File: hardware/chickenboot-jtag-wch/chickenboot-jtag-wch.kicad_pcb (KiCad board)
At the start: 2 copper layers, 29 x 18 mm, 27 parts, among them J1 USB_C_Receptacle_USB2.0, J2 Conn_01x03, J3 JTAG, J4 Conn_01x03, Q1 LP0404N3T5G, SW2 SW_Push, U1 CH32X035F8U6, U2 HT7533-1, U3 USBLC6-2P6, U4 IS25WP016D-JULE-TR, U5 IS25WP016D-JULE-TR

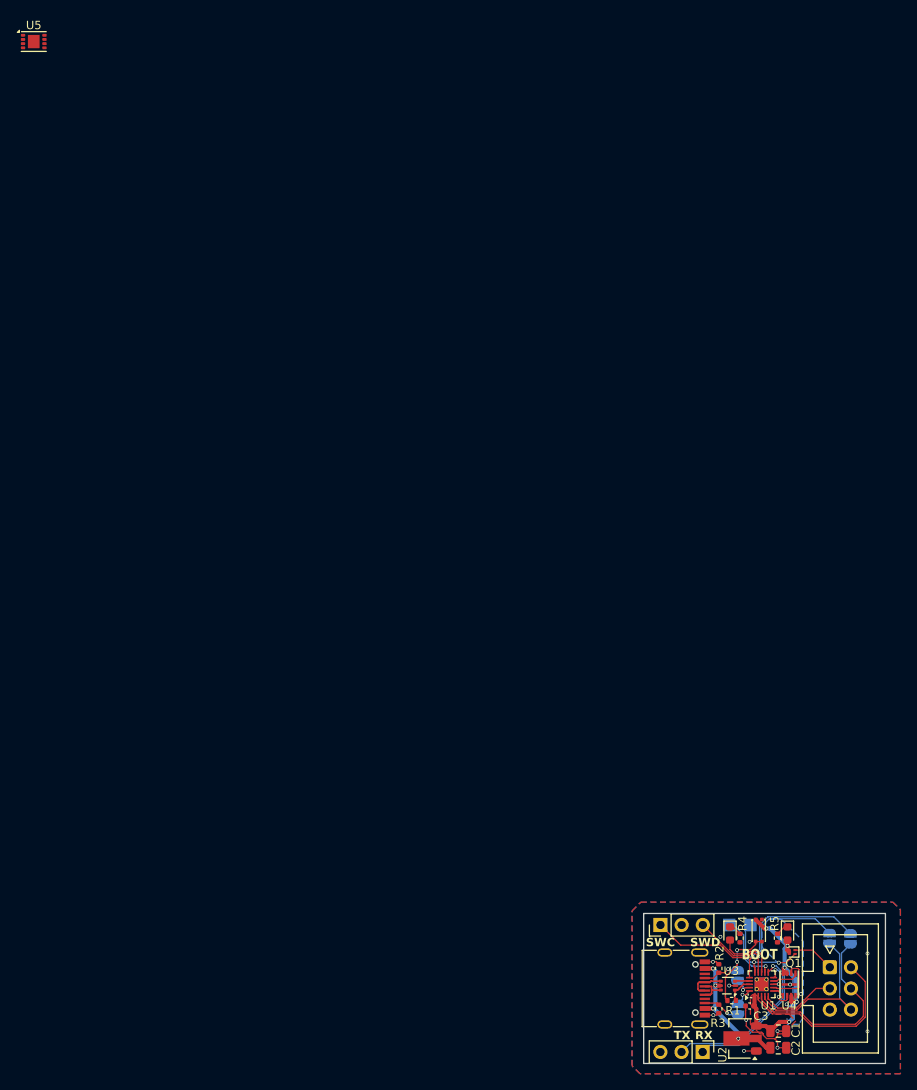
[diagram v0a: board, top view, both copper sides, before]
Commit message: add a decouliping capacitor to flash, a pullup to PMOS power control, and clean schematics
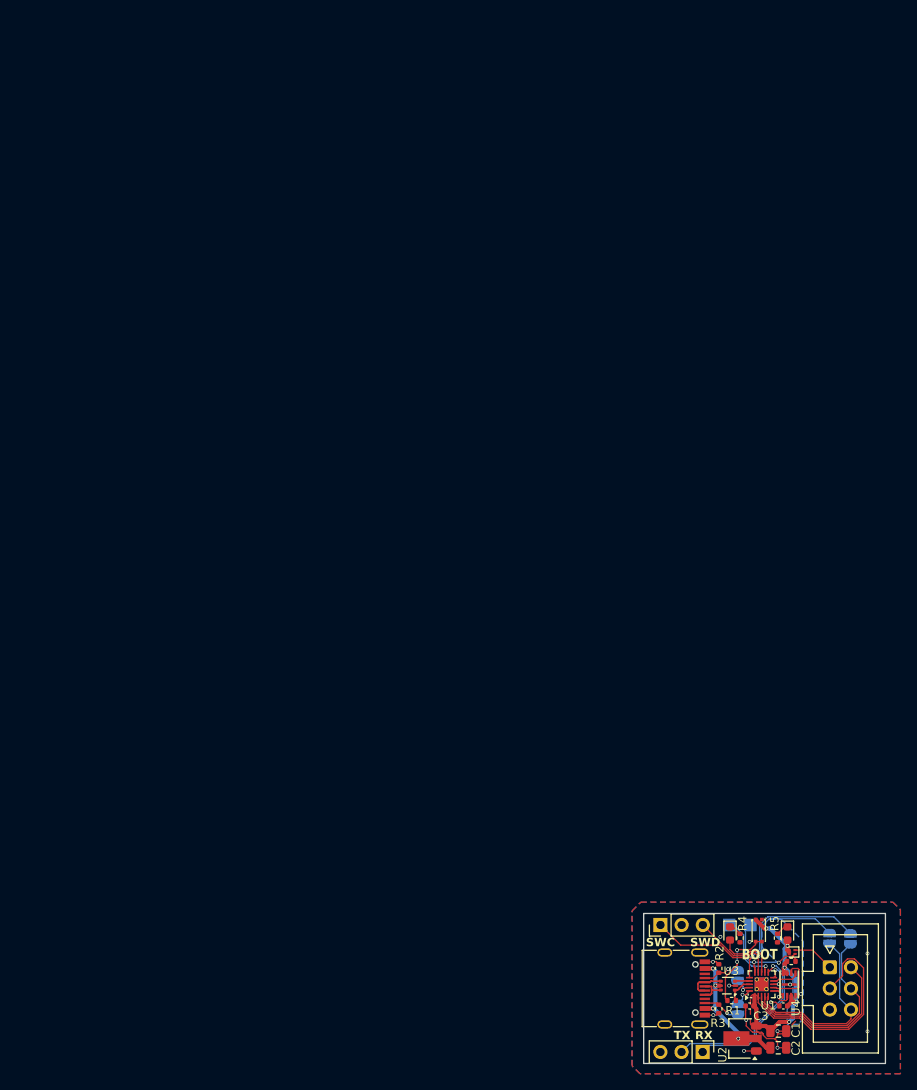
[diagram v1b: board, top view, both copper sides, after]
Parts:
- removed U5: IS25WP016D-JULE-TR, Package_SON:SON-8-1EP_3x2mm_P0.5mm_EP1.4x1.6mm
- added C4: .1uF, Capacitor_SMD:C_0402_1005Metric, F.Cu at (92.0, 117.2)
- added R6: 5.1K 1%, Resistor_SMD:R_0402_1005Metric, F.Cu at (93.0, 111.8)
- SW2: value SW_Push -> BOOT
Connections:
- net CC1 renamed /CC1
- net CC2 renamed /CC2
- net Net-(JP1-B) renamed /CC1_MCU
- net Net-(JP2-B) renamed /CC2_MCU
- net Net-(LED1-A) renamed /LED_STATUS
- U1 pad 2: JTAG_TMS -> JTAG_TDI
- U1 pad 3: JTAG_TCK -> JTAG_TMS
- U1 pad 4: JTAG_TDO -> JTAG_TCK
- U1 pad 5: JTAG_TDI -> JTAG_TDO
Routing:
- net JTAG_TDI: track 9.09 -> 27.9 mm
- net JTAG_TMS: track 23.0 -> 20.8 mm
- net +3V3: track 27.7 -> 29.3 mm
- net GND: track 17.7 -> 18.9 mm
- net JTAG_TDO: track 21.2 -> 22.3 mm
- net JTAG_TCK: track 24.4 -> 23.5 mm
- net /VTARGET_OFF: track 12.1 -> 12.8 mm
- net /RX: track 18.3 -> 18.9 mm
- net /TX: track 19.7 -> 20.4 mm
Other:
- board text added: "JTAG v0.1"
- board text removed: "JTAG v0.09"

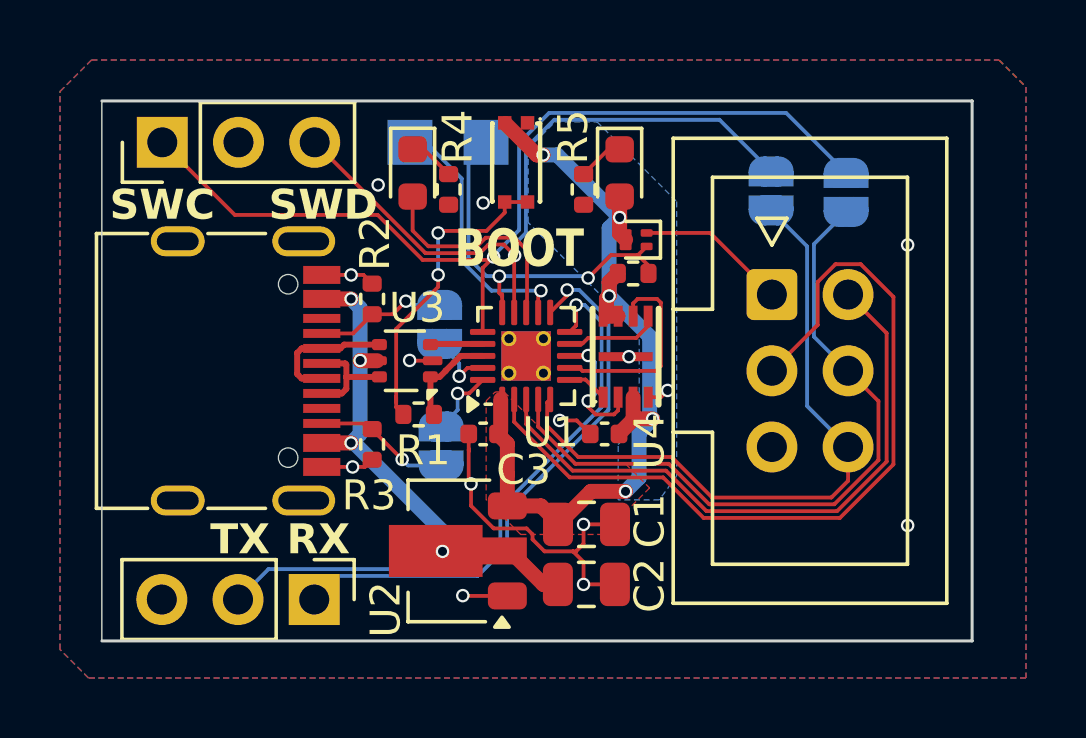
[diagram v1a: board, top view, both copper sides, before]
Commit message: change boards shape and fixes for manufacturability
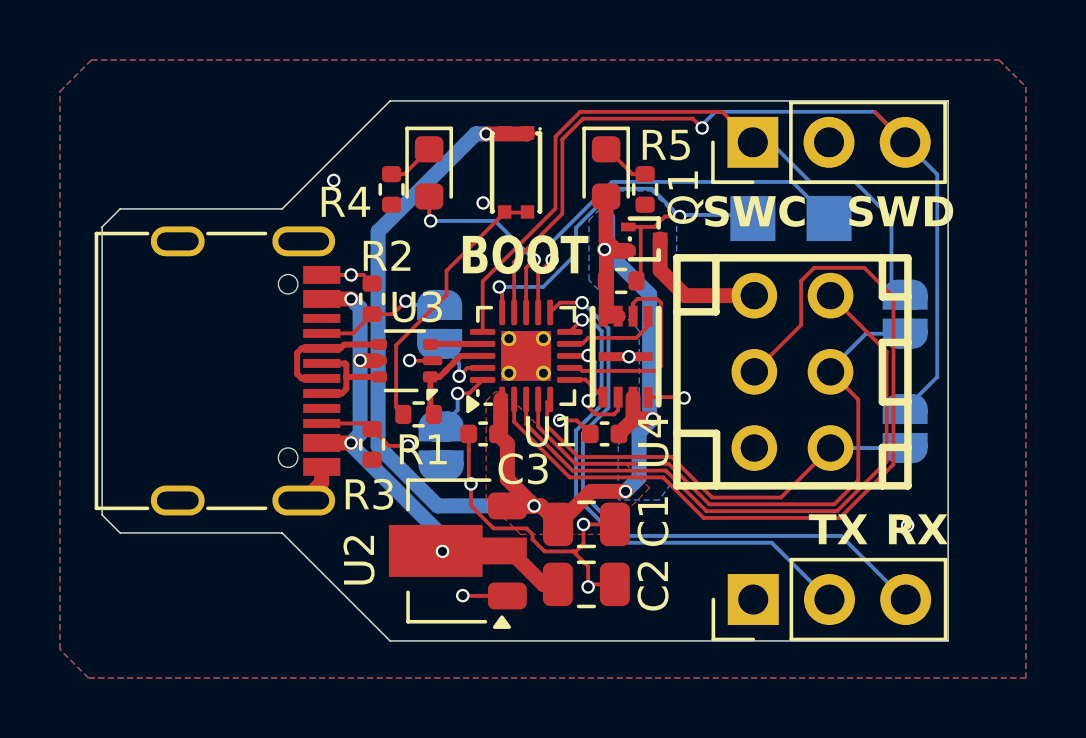
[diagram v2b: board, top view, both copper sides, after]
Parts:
- removed J3: JTAG, Connector_IDC:IDC-Header_2x03_P2.54mm_Vertical
- removed SW2: BOOT, easyeda2kicad:SW-SMD_4P-L2.5-W1.6-LS2.9_STI-055A12AX
- added CN1: 69168-106HLF, easyeda2kicad:CONN-TH_6P-P2.54_69168-X06, F.Cu at (98.3, 115.1)
- added SW1: SW_Push, easyeda2kicad:SW-SMD_4P-L2.5-W1.6-LS2.9_STI-055A12AX, F.Cu at (89.1, 108.4)
- Q1: value LP0404N3T5G -> WPM2093-3/TR; footprint Package_TO_SOT_SMD:SOT-883 -> easyeda2kicad:SOT-723_L1.2-W0.8-P0.80-LS1.2-BR
- moved J2 19.7 mm to (96.9, 107.4)
- moved J4 14.6 mm to (97.0, 122.7), turned to 90 degrees
- moved TP1 14.2 mm to (99.5, 110.0)
- moved TP2 9.25 mm to (96.9, 110.0)
- moved JP3 9.09 mm to (102.0, 117.0)
- moved JP4 4.51 mm to (102.0, 113.2)
- moved R5 2.05 mm to (93.4, 109.0)
- moved R4 1.90 mm to (84.9, 109.0)
- moved LED1 0.55 mm to (86.2, 108.5)
- moved R6 0.47 mm to (92.6, 112.1)
- moved LED2 0.45 mm to (92.1, 108.5)
- moved Q1 0.27 mm to (93.3, 110.7)
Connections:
- J4 pad 1: /RX -> GND
- J4 pad 3: GND -> /RX
- Q1 pad 2: TARGET_VCC -> +3V3
- Q1 pad 3: +3V3 -> TARGET_VCC
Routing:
- net +3V3: track 29.3 -> 47.2 mm
- net /SWCLK: track 31.7 -> 23.3 mm, vias 1 -> 0
- net JTAG_TDO: track 22.3 -> 14.6 mm
- net /SWDIO: track 23.4 -> 30.2 mm
- net /QSPI_CLOCK: track 8.84 -> 13.1 mm
- net JTAG_TCK: track 23.5 -> 20.0 mm
- net /TX: track 20.4 -> 17.1 mm
- net /VTARGET_OFF: track 12.8 -> 15.3 mm
- net /RX: track 18.9 -> 20.5 mm
- net Net-(R1-Pad2): track 10.6 -> 9.28 mm, vias 2 -> 0
- net /LED_STATUS: track 7.54 -> 6.68 mm, vias 0 -> 2
- net JTAG_TDI: track 27.9 -> 28.4 mm
- net GND: vias 14 -> 12
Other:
- board size 29 x 18 mm -> 28.2 x 18 mm

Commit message: fix vias and tracks to pass DFM
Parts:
- moved U4 0.13 mm to (92.8, 114.6)
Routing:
- net GND: track 18.9 -> 13.5 mm, vias 12 -> 13
- net /SWDIO: track 30.2 -> 29.2 mm, vias 1 -> 0
- net +3V3: track 47.2 -> 46.5 mm
- net JTAG_TDO: track 14.6 -> 15.3 mm
- net /TX: track 17.1 -> 17.7 mm
- net JTAG_TDI: track 28.4 -> 27.8 mm
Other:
- board size 28.2 x 18 mm -> 28.5 x 18 mm
